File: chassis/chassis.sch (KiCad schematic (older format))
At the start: 27 parts, among them J1 MicroD-15Pins, J10 MicroD-37Pins, J2 MicroD-15Pins, J200 Conn_01x04, J202 Conn_01x07, J203 MilSpec-91Pins, J3 MicroD-37Pins, J4 MicroD-37Pins, J5 MicroD-37Pins, J6 MicroD-37Pins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

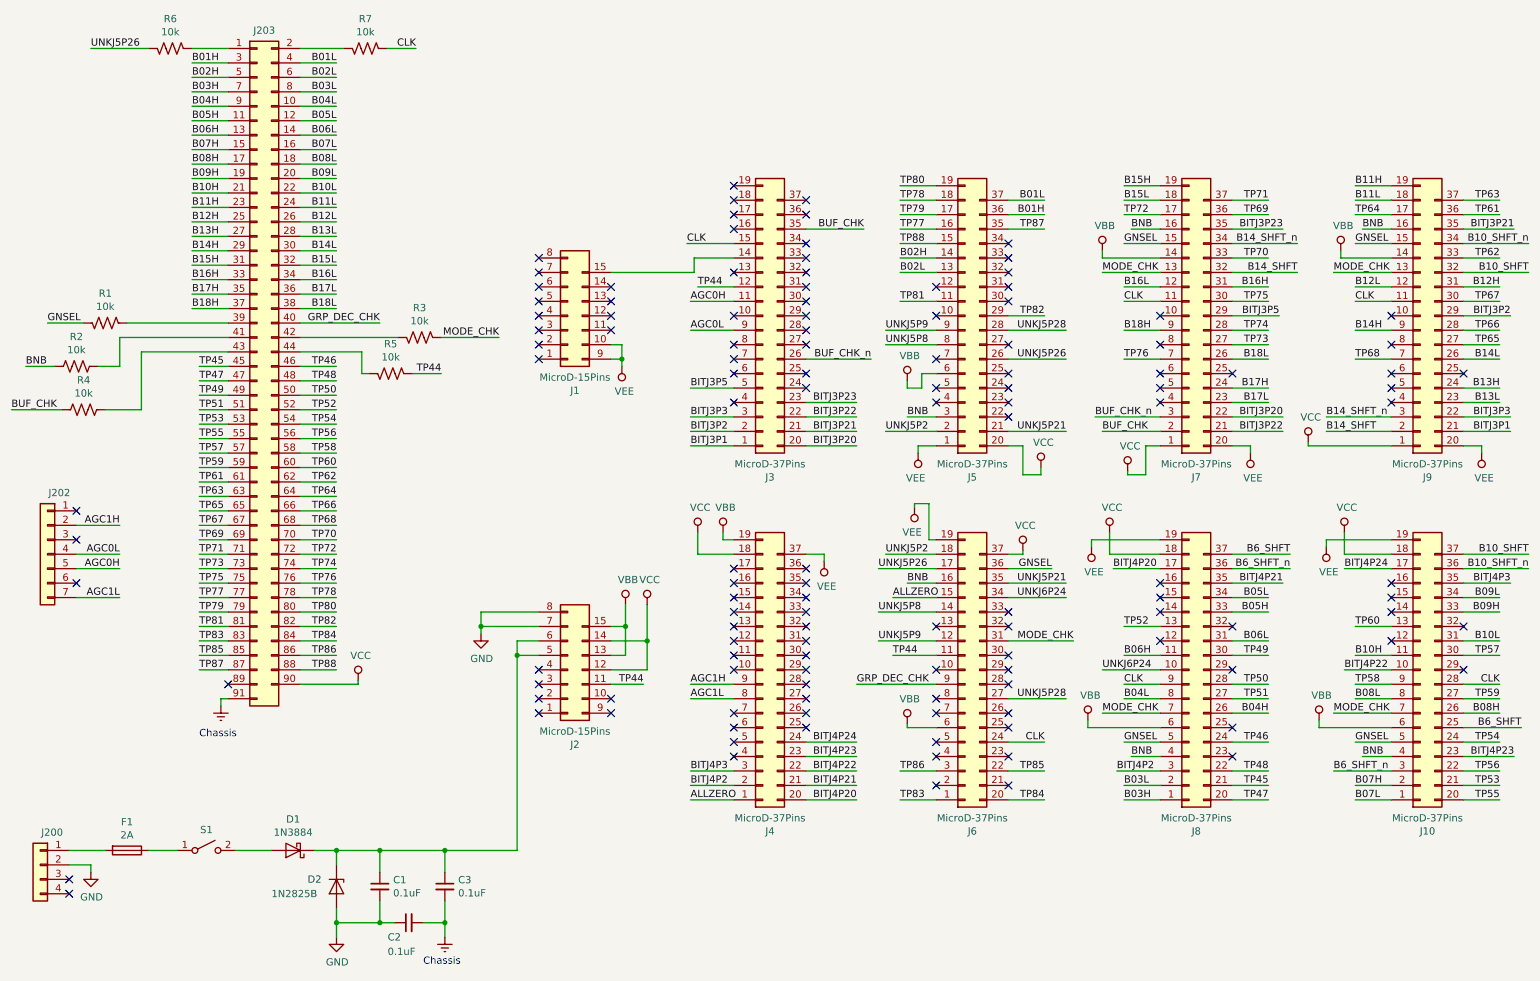
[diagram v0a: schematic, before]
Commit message: Eradicated net names taken from ME901-0666 -- the pinout was completely changed from early revs of that document.
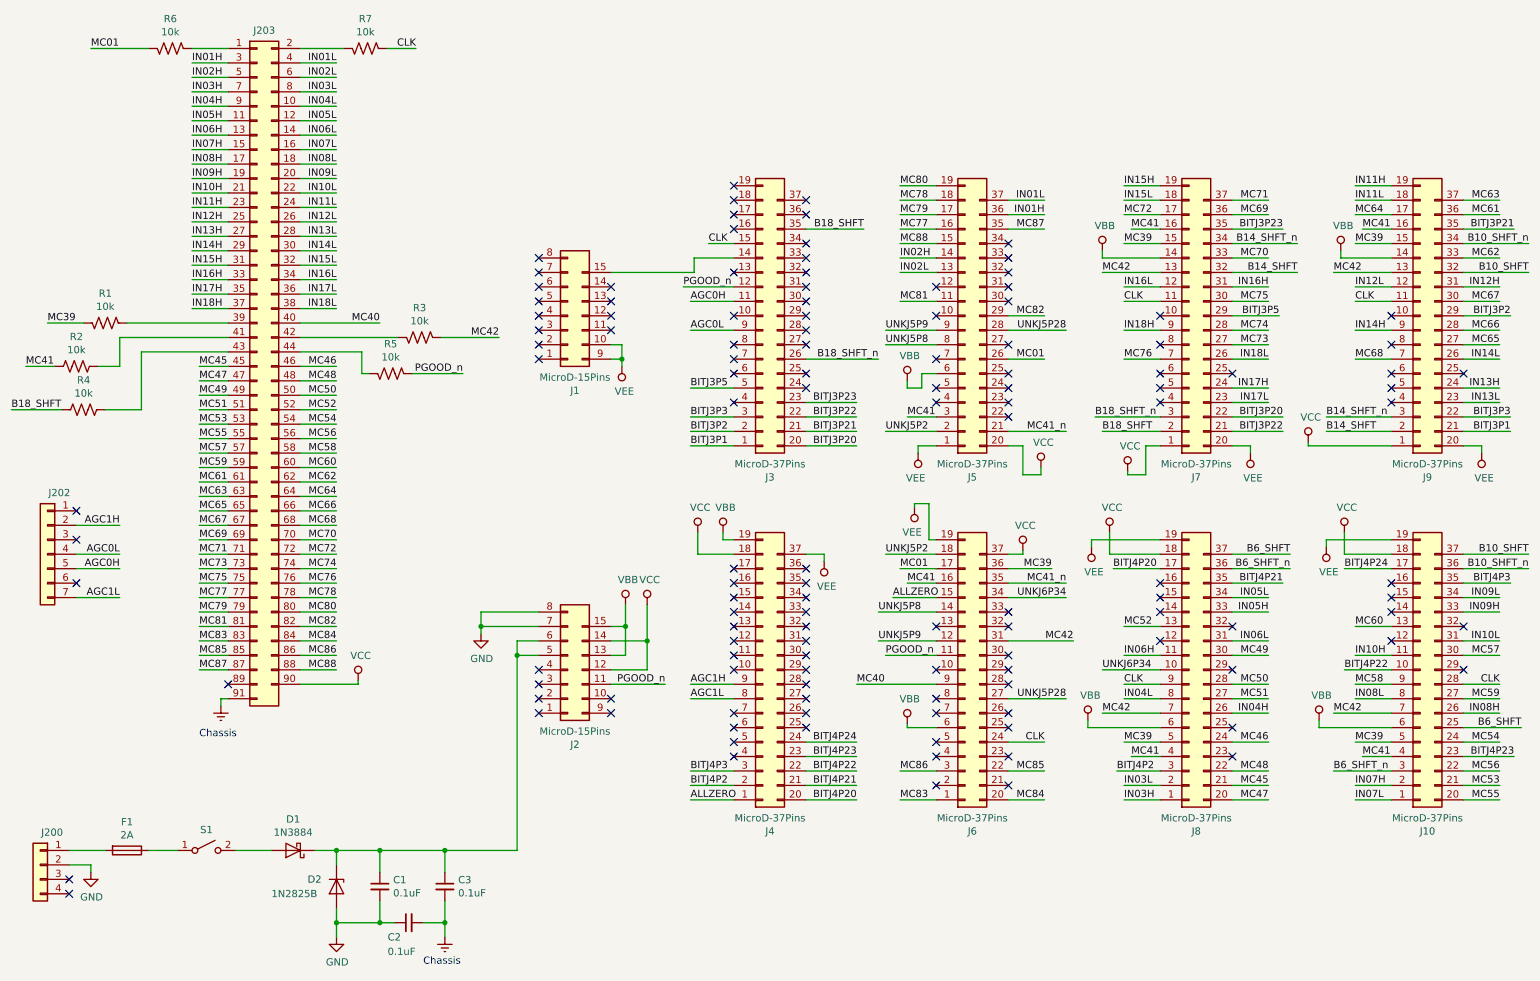
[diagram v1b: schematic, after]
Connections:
- net B01H renamed IN01H
- net B01L renamed IN01L
- net B02H renamed IN02H
- net B02L renamed IN02L
- net B03H renamed IN03H
- net B03L renamed IN03L
- net B04H renamed IN04H
- net B04L renamed IN04L
- net B05H renamed IN05H
- net B05L renamed IN05L
- net B06H renamed IN06H
- net B06L renamed IN06L
- net B07H renamed IN07H
- net B07L renamed IN07L
- net B08H renamed IN08H
- net B08L renamed IN08L
- net B09H renamed IN09H
- net B09L renamed IN09L
- net B10H renamed IN10H
- net B10L renamed IN10L
- net B11H renamed IN11H
- net B11L renamed IN11L
- net B12H renamed IN12H
- net B12L renamed IN12L
- net B13H renamed IN13H
- net B13L renamed IN13L
- net B14H renamed IN14H
- net B14L renamed IN14L
- net B15H renamed IN15H
- net B15L renamed IN15L
- net B16H renamed IN16H
- net B16L renamed IN16L
- net B17H renamed IN17H
- net B17L renamed IN17L
- net B18H renamed IN18H
- net B18L renamed IN18L
- net BNB renamed MC41
- net BUF_CHK renamed B18_SHFT
- net BUF_CHK_n renamed B18_SHFT_n
- net GNSEL renamed MC39
- net GRP_DEC_CHK renamed MC40
- net MODE_CHK renamed MC42
- net TP44 renamed PGOOD_n
- net TP45 renamed MC45
- net TP46 renamed MC46
- net TP47 renamed MC47
- net TP48 renamed MC48
- net TP49 renamed MC49
- net TP50 renamed MC50
- net TP51 renamed MC51
- net TP52 renamed MC52
- net TP53 renamed MC53
- net TP54 renamed MC54
- net TP55 renamed MC55
- net TP56 renamed MC56
- net TP57 renamed MC57
- net TP58 renamed MC58
- net TP59 renamed MC59
- net TP60 renamed MC60
- net TP61 renamed MC61
- net TP62 renamed MC62
- net TP63 renamed MC63
- net TP64 renamed MC64
- net TP65 renamed MC65
- net TP66 renamed MC66
- net TP67 renamed MC67
- net TP68 renamed MC68
- net TP69 renamed MC69
- net TP70 renamed MC70
- net TP71 renamed MC71
- net TP72 renamed MC72
- net TP73 renamed MC73
- net TP74 renamed MC74
- net TP75 renamed MC75
- net TP76 renamed MC76
- net TP77 renamed MC77
- net TP78 renamed MC78
- net TP79 renamed MC79
- net TP80 renamed MC80
- net TP81 renamed MC81
- net TP82 renamed MC82
- net TP83 renamed MC83
- net TP84 renamed MC84
- net TP85 renamed MC85
- net TP86 renamed MC86
- net TP87 renamed MC87
- net TP88 renamed MC88
- net UNKJ5P21 renamed MC41_n
- net UNKJ5P26 renamed MC01
- net UNKJ6P24 renamed UNKJ6P34

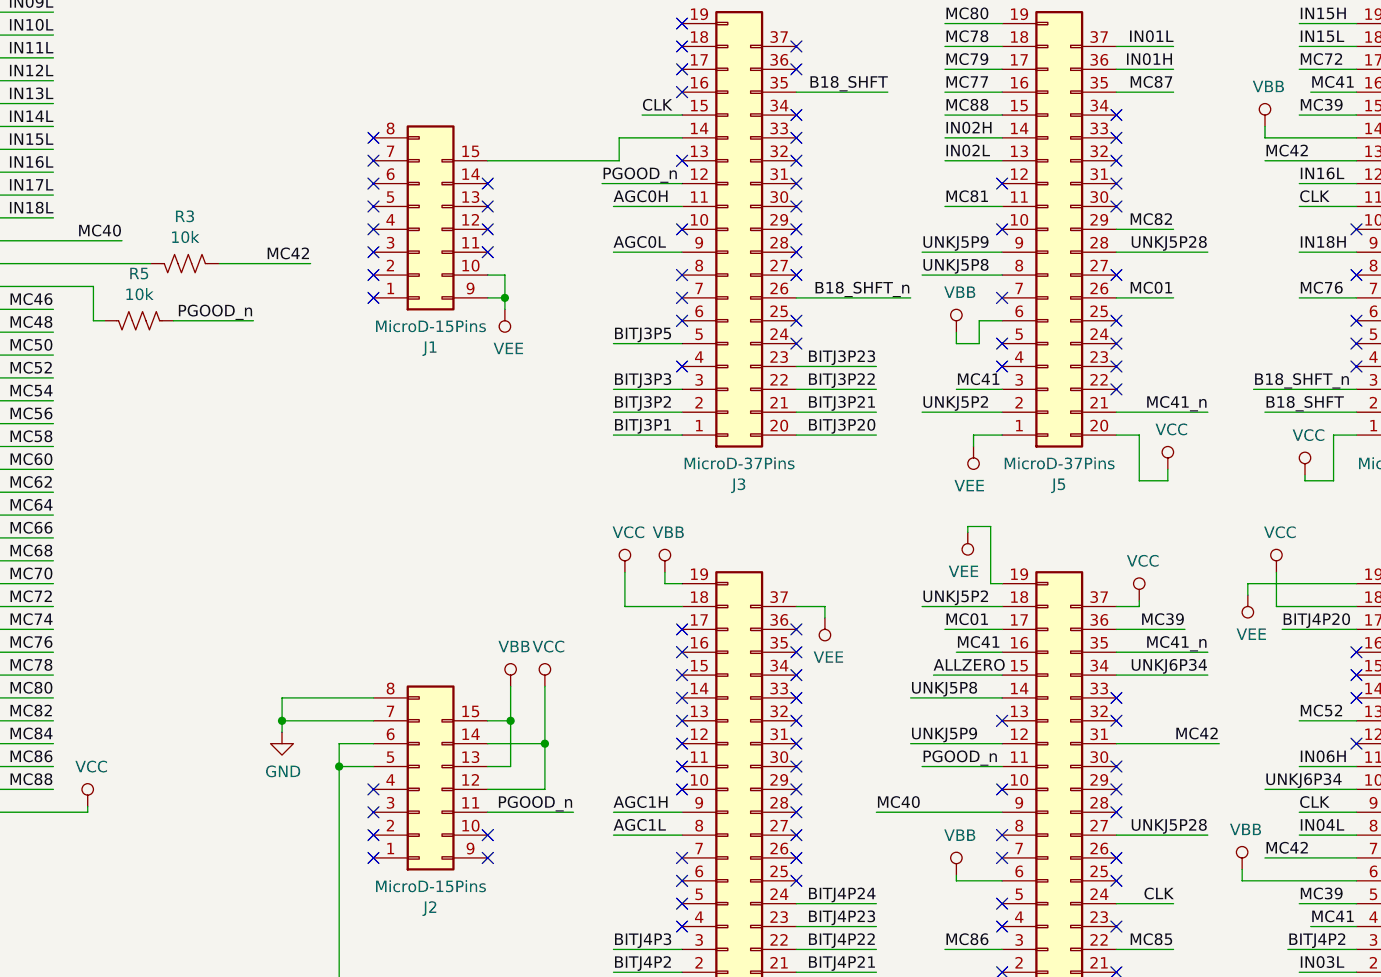
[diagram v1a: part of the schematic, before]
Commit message: Corrected a schematic error in module 3 board 1, which now makes much more sense. Also renamed the power good net to VFAIL.
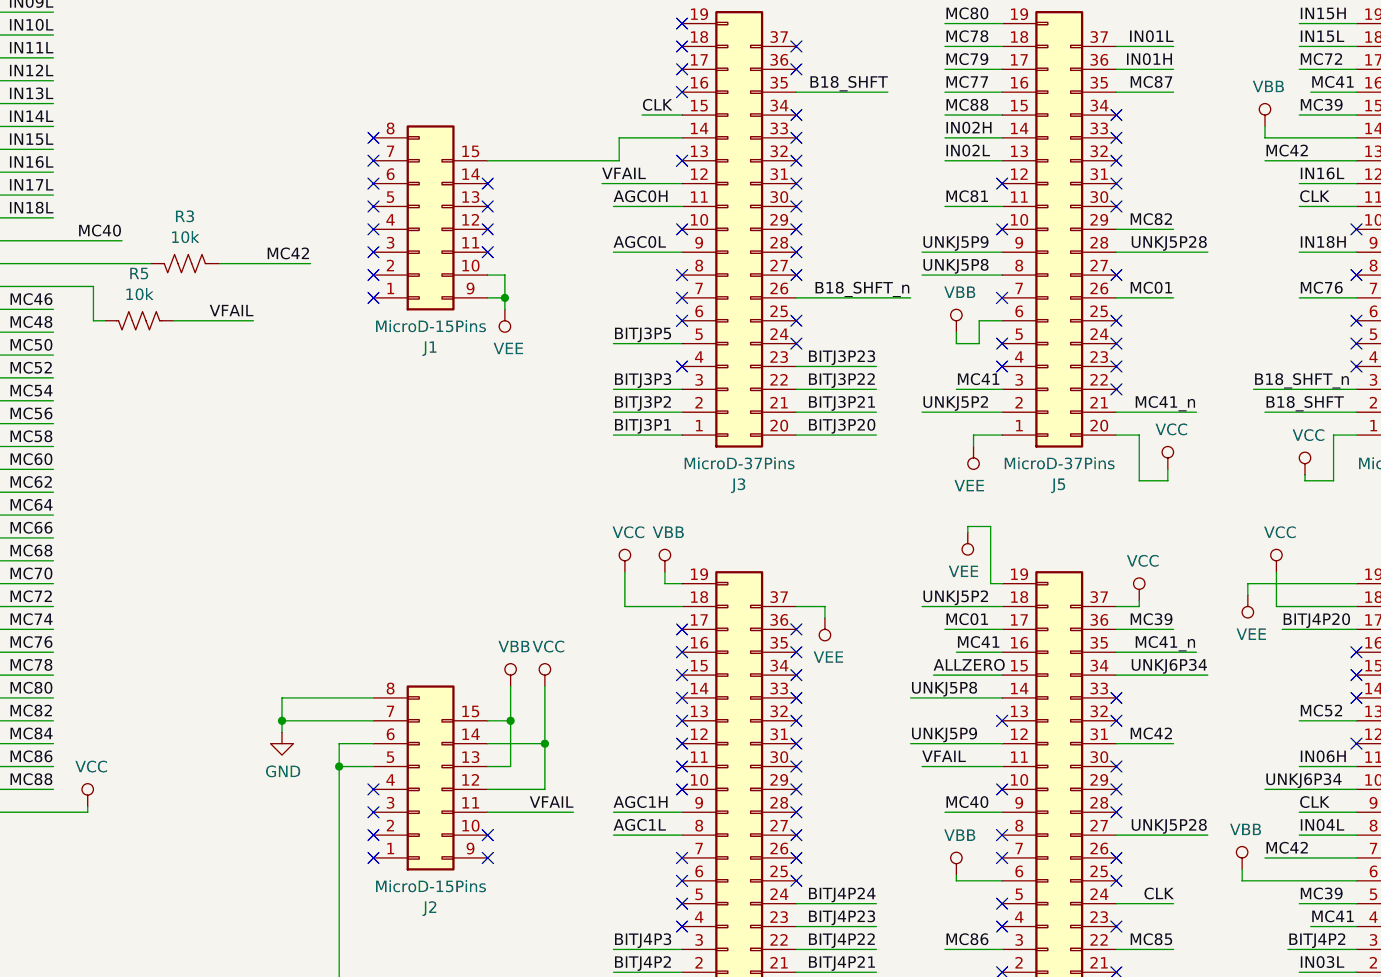
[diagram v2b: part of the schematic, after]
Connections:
- net PGOOD_n renamed VFAIL
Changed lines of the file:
@@
 	3425 3050 3775 3050
 Text Label 3775 3050 2    50   ~ 0
-PGOOD_n
+VFAIL
 Wire Wire Line
 	2650 2900 3075 2900
@@
 	10700 1950 10950 1950
 Text Label 5300 2450 0    50   ~ 0
-PGOOD_n
+VFAIL
 Wire Wire Line
 	5650 2450 5300 2450
@@
 	7050 6000 6800 6000
 Text Label 6700 5000 0    50   ~ 0
-PGOOD_n
+VFAIL
 Wire Wire Line
 	7050 5000 6700 5000
 Wire Wire Line
-	8000 4900 7550 4900
-Text Label 8000 4900 2    50   ~ 0
+	7800 4900 7550 4900
+Text Label 7800 4900 2    50   ~ 0
 MC42
 Text Label 6850 4500 0    50   ~ 0
@@
 Wire Wire Line
 	7050 4500 6850 4500
-Text Label 7850 4400 2    50   ~ 0
+Text Label 7800 4400 2    50   ~ 0
 MC39
-Text Label 6500 5200 0    50   ~ 0
+Text Label 6800 5200 0    50   ~ 0
 MC40
 Wire Wire Line
-	7050 5200 6500 5200
-Wire Wire Line
-	7850 4400 7550 4400
+	7050 5200 6800 5200
+Wire Wire Line
+	7800 4400 7550 4400
 $Comp
 L gn_buffer:MicroD-37Pins J6
@@
 	4800 5200 5175 5200
 Text Label 5175 5200 2    50   ~ 0
-PGOOD_n
+VFAIL
 Wire Wire Line
 	4800 5000 4900 5000
@@
 Text Label 6700 2850 0    50   ~ 0
 UNKJ5P8
-Text Label 7950 3450 2    50   ~ 0
+Text Label 7900 3450 2    50   ~ 0
 MC41_n
 Wire Wire Line
-	7550 3450 7950 3450
+	7550 3450 7900 3450
 Wire Wire Line
 	7650 3750 7650 3550
@@
 Wire Wire Line
 	6950 3050 7050 3050
-Text Label 7950 4500 2    50   ~ 0
+Text Label 7900 4500 2    50   ~ 0
 MC41_n
 Wire Wire Line
-	7550 4500 7950 4500
+	7550 4500 7900 4500
 Wire Wire Line
 	7550 2950 7800 2950

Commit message: Initial schematic for module 4, board 1, plus lots of associated net name updates. The shift register is done, but a lot of surrounding NOR logic still needs to be untangled.
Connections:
- net ALLZERO renamed BUFSET
- net B10_SHFT renamed BUF08
- net B10_SHFT_n renamed BUF08_n
- net B14_SHFT renamed BUF12
- net B14_SHFT_n renamed BUF12_n
- net B18_SHFT renamed BUF16
- net B18_SHFT_n renamed BUF16_n
- net B6_SHFT renamed BUF04
- net B6_SHFT_n renamed BUF04_n
- net BITJ3P1 renamed B12SET
- net BITJ3P2 renamed B10SET
- net BITJ3P20 renamed B15SET
- net BITJ3P21 renamed B09SET
- net BITJ3P22 renamed B16SET
- net BITJ3P23 renamed B13SET
- net BITJ3P3 renamed B11SET
- net BITJ3P5 renamed B14SET
- net BITJ4P2 renamed B01SET
- net BITJ4P20 renamed B04SET
- net BITJ4P21 renamed B03SET
- net BITJ4P22 renamed B06SET
- net BITJ4P23 renamed B05SET
- net BITJ4P24 renamed B08SET
- net BITJ4P3 renamed B07SET
- net UNKJ6P34 renamed B02SET
